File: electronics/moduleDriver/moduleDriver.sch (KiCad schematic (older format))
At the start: 31 parts, among them J1 Screw_Terminal_01x03, U1 Mega2560Shield, U10 ULN2003AModule, U11 ULN2003AModule, U12 ULN2003AModule, U13 ULN2003AModule, U14 SSD1306_I2C, U15 INA219_Breakout, U2 ULN2003AModule, U3 ULN2003AModule, U4 ULN2003AModule, U5 ULN2003AModule, U6 ULN2003AModule, U7 ULN2003AModule, U8 ULN2003AModule, U9 ULN2003AModule

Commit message: More schematic progress
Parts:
- removed JP?: 3V_VCC, symbol Device:Jumper_NO_Small
- removed JP?: 5V_VCC, symbol Device:Jumper_NO_Small
- added J?: Screw_Terminal_01x03, symbol Connector:Screw_Terminal_01x03
- added J? (x3): Conn_01x12_Male, symbol Connector:Conn_01x12_Male
- added R? (x12): 47k, symbol Device:R_Small
- added U?: RS485Module, symbol RS485Module:RS485Module
- added U?: LevelShifterModule, symbol LevelShifterModule:LevelShifterModule
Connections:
- net labels added: IOVCC, RS485_DRIVE_EN, RX_5V, TX_5V
- net labels removed: VCC
- wire segments 403 -> 517
- no-connect marks 49 -> 51
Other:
- note added: "IOVCC is sourced by (through) \nESP32 module when present."
- note added: "IOVCC is sourced by (through) \nMega 2560 when present."
- note added: "Resistors only for ESP32"
- moved on the sheet: J1, JP1, U1, U10, U11, U12, U13, U14, U15, U2, U3, U4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

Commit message: More schematic cleanup
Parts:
- added JP?: RX 3.3V, symbol Jumper:SolderJumper_2_Open
- added JP?: TX 3.3V, symbol Jumper:SolderJumper_2_Open
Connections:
- net RS485_DRIVE_EN: now also U?.5 (GPIO17), U?.5 (LV3); no longer U?.DE, U?.RE
- net RX: now also JP?.1 (A); no longer J?.2 (Pin_2), U1.D0
- net RX_5V: now also J?.2 (Pin_2), U1.D0, JP?.2 (B)
- net TX: now also JP?.1 (A); no longer J?.1 (Pin_1), U1.D1
- net TX_5V: now also J?.1 (Pin_1), U1.D1, JP?.2 (B)
- net RS485_DRIVE_EN_5V: now reaches U1.D4
- net RS485_DRIVE_EN_5V: now also U?.8 (HV3), U?.DE, U?.RE
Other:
- note added: "MCU Option 1: Mega2560 + SSD1306 OLED"
- note added: "MCU Option 2: TTGO T-Display (ESP32)"
- note added: "MCU Option 3: ESP32 D1 Mini"
- note added: "Motor Driver Modules"
- note added: "Only populate for shift register chaining"
- note added: "Optional: Current sense"
- note added: "Optional: RS485 comms/UART voltage shifting"
- note added: "Populate when using ESP32 MCU"
- note added: "Resistors only for ESP32\n(47k)"
- note added: "Sensor Connectors"
- note removed: "Resistors only for ESP32"
- moved on the sheet: JP1, U1, U14, U15, U?

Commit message: ESP32 D1 pinout connections
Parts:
- added J?: SR CHAIN IN, symbol Connector:Screw_Terminal_01x06
- added J?: SR CHAIN OUT, symbol Connector:Screw_Terminal_01x06
- J1: value Screw_Terminal_01x03 -> Power In
- J?: value Screw_Terminal_01x03 -> UART
- J?: value Conn_01x12_Male -> SENSOR
- J?: value Conn_01x12_Male -> IOVCC
- J?: value Conn_01x12_Male -> GND
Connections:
- net +5V: now also U?.36 (5V/5V)
- net CLOCK: now also U?.8 (GPIO18/D5), J?.2 (Pin_2)
- net CLOCK_IN: now also J?.2 (Pin_2)
- net DISP_BLK: now also U?.23 (GPIO27)
- net DISP_CLK: now also U?.25 (GPIO25)
- net DISP_CS: now also U?.33 (GPIO0)
- net DISP_DC: now also U?.27 (GPIO32)
- net DISP_MOSI: now also U?.18 (GPIO13)
- net DISP_RES: now also U?.31 (GPIO4), U?.9 (GPIO33)
- net GND: now also U?.1 (GND), U?.21 (GND), U?.34 (GND/GND)
- net IOVCC: now also U?.16 (3V3/3V3)
- net MOTOR_DATA: now also U?.12 (GPIO23/D7)
- net MOTOR_DATA_IN: now also J?.1 (Pin_1)
- net MOTOR_DATA_OUT: now also J?.1 (Pin_1)
- net MOTOR_LATCH: now also U?.6 (GPIO26/D0), J?.3 (Pin_3)
- net MOTOR_LATCH_IN: now also J?.3 (Pin_3)
- net MOTOR_OE: now also U?.32 (GPIO16/D4), J?.4 (Pin_4)
- net MOTOR_OE_IN: now also J?.4 (Pin_4)
- net RS485_DRIVE_EN: now also U?.30 (GPIO17/D3)
- net RX: now also U?.24 (GPIO3/RX)
- net SCL: now also U?.26 (GPIO22/D1)
- net SDA: now also U?.28 (GPIO21/D2)
- net SENSOR_DATA: now also U?.10 (GPIO19/D6), J?.5 (Pin_5)
- net SENSOR_DATA_IN: now also J?.5 (Pin_5)
- net SENSOR_LATCH: now also U?.14 (GPIO5/D8), J?.6 (Pin_6)
- net SENSOR_LATCH_IN: now also J?.6 (Pin_6)
- net TX: now also U?.22 (GPIO1/TX)
- no-connect marks 51 -> 57
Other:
- note added: "Connectors"
- note added: "ESP32/ESP8266 IO Support"
- note added: "MCU Option 3: ESP32/ESP8266 D1 Mini"
- note added: "Optional: Shift register chaining support"
- note removed: "MCU Option 3: ESP32 D1 Mini"
- note removed: "Only populate for shift register chaining"
- note removed: "Populate when using ESP32 MCU"
- moved on the sheet: J1, J?, JP?, R?, U10, U11, U12, U13, U15, U2, U3, U4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

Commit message: More schematic progress, comments
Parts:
- added JP4: Current Sense Bypass, symbol Device:Jumper_NO_Small
- J1: symbol Connector:Screw_Terminal_01x03 -> screw_terminal_01x03_power_output:Screw_Terminal_01x03
- gave numbers to parts that had none: 34
- renumbered U9 to U10, U15 to U11, U10 to U12, U11 to U13, U12 to U14, U13 to U15, U14 to U2, U2 to U3, U3 to U4, U4 to U5, U5 to U6, U6 to U7, U7 to U8, U8 to U9
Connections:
- net +3V3 is gone; now on net IOVCC: U16.3 (LV)
- net +12V: now also JP4.1
- net +12V_Monitored: now also JP4.2
- net +5V: now also U1.5V
- net IOVCC: now also U1.IOREF; no longer U1.5V
- net TX_5V: no longer J2.1 (Pin_1), U1.D1, U17.DI
- net RX_5V renamed RX_EXT
- new net TX_EXT: J2.1 (Pin_1), U1.D1, U17.DI
- no-connect marks 57 -> 81
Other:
- note added: "Configuration options:\n\nMega 2560: DNP U16; External RX/TX = 5V; do not use JP2/JP3\n\nESP32/ESP8266:\n For 5V RX/TX: Use U16; do not use JP2/JP3\n For 3.3V RX/TX: DNP U16; set JP2 and JP3"
- note added: "For compatibility with ESP8266, all critical IO\nuses the inner pins; optional IO (e.g. display)\ncan use the outer pins (only present for ESP32\nmodules)"
- note added: "IOVCC is sourced by\nESP32 module when present."
- note added: "IOVCC is sourced by\nMega 2560 when present."
- note added: "RS485 Requires 5V RX/TX - for ESP32/ESP8266 must use U16"
- note removed: "IOVCC is sourced by (through) \nESP32 module when present."
- note removed: "IOVCC is sourced by (through) \nMega 2560 when present."
- moved on the sheet: JP2, JP3, U16, U17

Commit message: Add some footprints and attach to schematic
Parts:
- added U30: ST7789_240x240, ST7789:ST7789_240x240, symbol LCD:ST7789_240x240
- J1, J2: footprint (none) -> TerminalBlock:TerminalBlock_bornier-3_P5.08mm
- J3, J4, J5: footprint (none) -> Connector_PinHeader_2.54mm:PinHeader_1x12_P2.54mm_Vertical
- J6, J7: footprint (none) -> TerminalBlock_TE-Connectivity:TerminalBlock_TE_282834-6_1x06_P2.54mm_Horizontal
- JP1, JP4: footprint (none) -> Connector_PinHeader_2.54mm:PinHeader_1x02_P2.54mm_Vertical
- JP2, JP3: footprint (none) -> Jumper:SolderJumper-2_P1.3mm_Open_RoundedPad1.0x1.5mm
- R1, R10, R11, R12, R2, R3, R4, R5, R6, R7, R8, R9: footprint (none) -> Resistor_THT:R_Axial_DIN0204_L3.6mm_D1.6mm_P1.90mm_Vertical
- U1: footprint (none) -> Mega2560Shield:Mega2560Shield
- U10, U12, U13, U14, U15, U3, U4, U5, U6, U7, U8, U9: footprint (none) -> ULN2003AModule:ULN2003AModule
- U18: footprint (none) -> ESP32:T-DISPLAY
- U2: footprint (none) -> Connector_PinSocket_2.54mm:PinSocket_1x04_P2.54mm_Vertical
- U20, U21: footprint MODULE -> Package_DIP:DIP-16_W7.62mm
- U22: value ST7789_IPS -> ST7789_80x160; footprint (none) -> ST7789:ST7789_80x160; symbol LCD:ST7789_IPS -> LCD:ST7789_80x160
- U23: footprint (none) -> ESP32:D1_32
- U24, U25, U26, U27, U28, U29: footprint (none) -> Package_DIP:DIP-16_W7.62mm
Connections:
- net +12V_Monitored: no longer U11.5 (VIN-)
- net DISP_BLK: now also U30.BLK
- net DISP_CLK: now also U30.SCL (SCL(CLK))
- net DISP_DC: now also U30.DC
- net DISP_MOSI: now also U30.SDA (SDA_(MOSI))
- net DISP_RES: now also U30.RES
- net GND: now also U30.GND
- net IOVCC: now also U30.VCC
- no-connect marks 81 -> 82
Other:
- note added: "47k. DNP for Mega 2560"
- note added: "IOVCC is sourced by the MCU\nmodule that's inserted, at the\nappropriate IO voltage\n(3.3V or 5V)"
- note removed: "IOVCC is sourced by\nESP32 module when present."
- note removed: "IOVCC is sourced by\nMega 2560 when present."
- note removed: "Resistors only for ESP32\n(47k)"
- moved on the sheet: U22

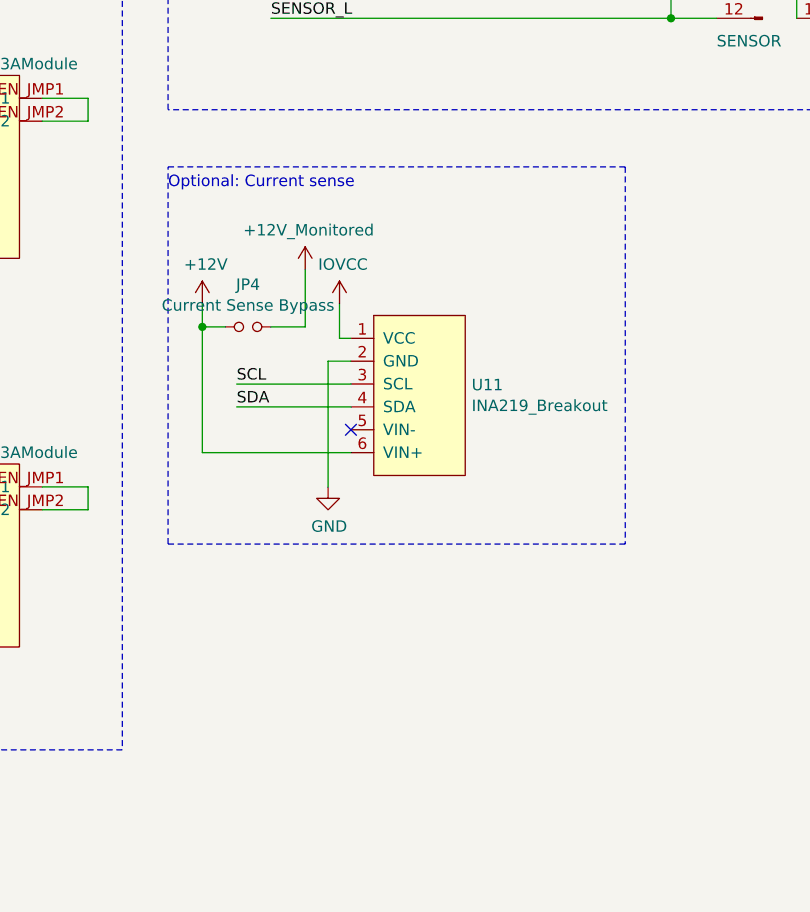
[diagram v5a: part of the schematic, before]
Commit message: Current sensor updates
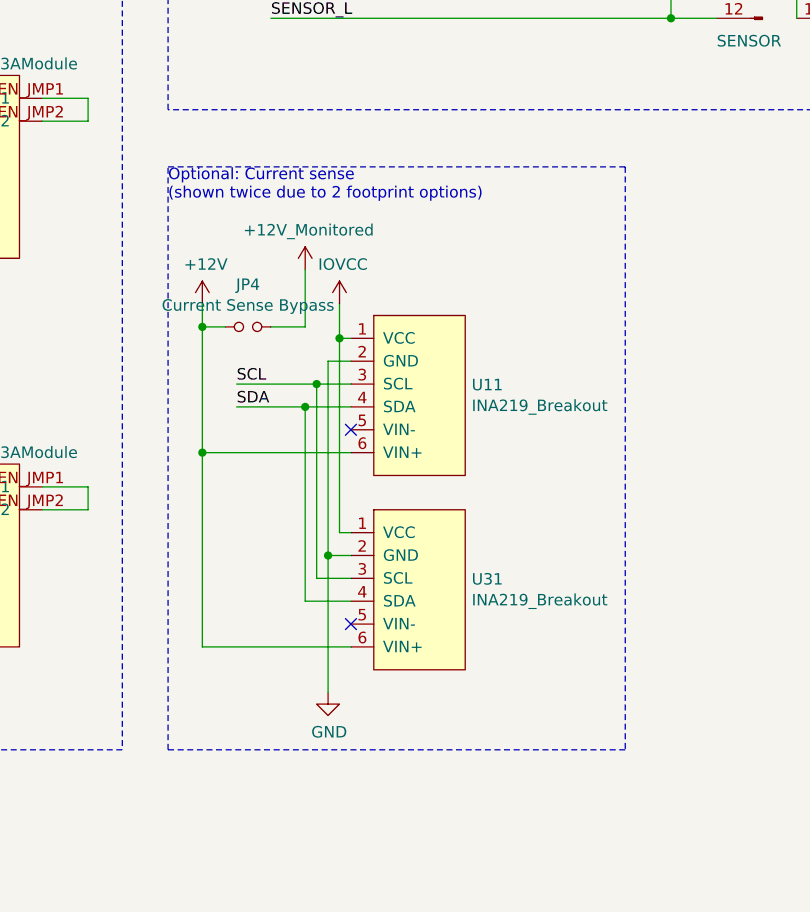
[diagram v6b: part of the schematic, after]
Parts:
- added U31: INA219_Breakout, INA219:INA219_SMALL, symbol INA219_Breakout:INA219_Breakout
- U11: footprint (none) -> INA219:INA219_SMALL
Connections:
- net +12V: now also U31.6 (VIN+)
- net GND: now also U31.2 (GND)
- net IOVCC: now also U31.1 (VCC)
- net SCL: now also U31.3 (SCL)
- net SDA: now also U31.4 (SDA)
- no-connect marks 82 -> 83
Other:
- note added: "Optional: Current sense\n(shown twice due to 2 footprint options)"
- note removed: "Optional: Current sense"
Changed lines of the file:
@@
 F 0 "U11" H 10528 5996 50  0000 L CNN
 F 1 "INA219_Breakout" H 10528 5905 50  0000 L CNN
-F 2 "" H 10000 6000 50  0001 C CNN
+F 2 "INA219:INA219_SMALL" H 10000 6000 50  0001 C CNN
 F 3 "" H 10000 6000 50  0001 C CNN
 	1    10300 5950
@@
 Wire Wire Line
 	10000 5800 9900 5800
-Wire Wire Line
-	9900 5800 9900 6350
 $Comp
 L power:GND #PWR035
 U 1 1 5F2DBE8C
-P 9900 6350
-F 0 "#PWR035" H 9900 6100 50  0001 C CNN
-F 1 "GND" H 9905 6177 50  0000 C CNN
-F 2 "" H 9900 6350 50  0001 C CNN
-F 3 "" H 9900 6350 50  0001 C CNN
-	1    9900 6350
+P 9900 7250
+F 0 "#PWR035" H 9900 7000 50  0001 C CNN
+F 1 "GND" H 9905 7077 50  0000 C CNN
+F 2 "" H 9900 7250 50  0001 C CNN
+F 3 "" H 9900 7250 50  0001 C CNN
+	1    9900 7250
 	1    0    0    -1
 $EndComp
@@
 SCL
 Wire Wire Line
-	10000 5900 9500 5900
-Wire Wire Line
-	10000 6000 9500 6000
+	10000 5900 9850 5900
+Wire Wire Line
+	10000 6000 9800 6000
 Text Label 19700 2800 2    50   ~ 0
 RX_EXT
@@
 Wire Notes Line
 	9200 4700 9200 2250
-Text Notes 9200 5050 0    50   ~ 0
-Optional: Current sense
+Text Notes 9200 5100 0    50   ~ 0
+Optional: Current sense\n(shown twice due to 2 footprint options)
 Wire Notes Line
 	9200 4950 11200 4950
-Wire Notes Line
-	11200 4950 11200 6600
-Wire Notes Line
-	11200 6600 9200 6600
-Wire Notes Line
-	9200 6600 9200 4950
 $Comp
 L Connector:Screw_Terminal_01x06 J6
@@
 	9800 5400 9800 5650
 Wire Wire Line
-	9350 6200 10000 6200
-Wire Wire Line
 	9350 5550 9350 5650
 $Comp
@@
 Wire Wire Line
 	20900 12750 20900 13300
+$Comp
+L INA219_Breakout:INA219_Breakout U31
+U 1 1 5FB8DCED
+P 10300 6800
+F 0 "U31" H 10528 6846 50  0000 L CNN
+F 1 "INA219_Breakout" H 10528 6755 50  0000 L CNN
+F 2 "INA219:INA219_SMALL" H 10000 6850 50  0001 C CNN
+F 3 "" H 10000 6850 50  0001 C CNN
+	1    10300 6800
+	1    0    0    -1
+$EndComp
+Wire Wire Line
+	9950 5700 9950 6550
+Wire Wire Line
+	9950 6550 10000 6550
+Connection ~ 9950 5700
+Wire Wire Line
+	9900 6650 10000 6650
+Wire Wire Line
+	9900 5800 9900 6650
+Wire Wire Line
+	9900 6650 9900 7250
+Connection ~ 9900 6650
+Wire Wire Line
+	9850 5900 9850 6750
+Wire Wire Line
+	9850 6750 10000 6750
+Connection ~ 9850 5900
+Wire Wire Line
+	9850 5900 9500 5900
+Wire Wire Line
+	9800 6000 9800 6850
+Wire Wire Line
+	9800 6850 10000 6850
+Connection ~ 9800 6000
+Wire Wire Line
+	9800 6000 9500 6000
+NoConn ~ 10000 6950
+Wire Wire Line
+	9350 6200 10000 6200
+Wire Wire Line
+	9350 6200 9350 7050
+Wire Wire Line
+	9350 7050 10000 7050
+Connection ~ 9350 6200
+Wire Notes Line
+	11200 4950 11200 7500
+Wire Notes Line
+	11200 7500 9200 7500
+Wire Notes Line
+	9200 7500 9200 4950
 $EndSCHEMATC

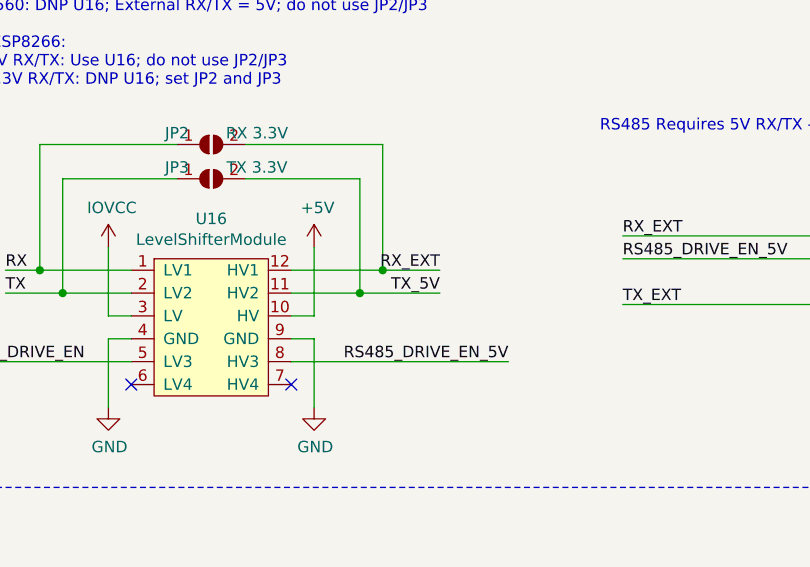
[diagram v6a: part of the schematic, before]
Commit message: Add RS485 module footprint
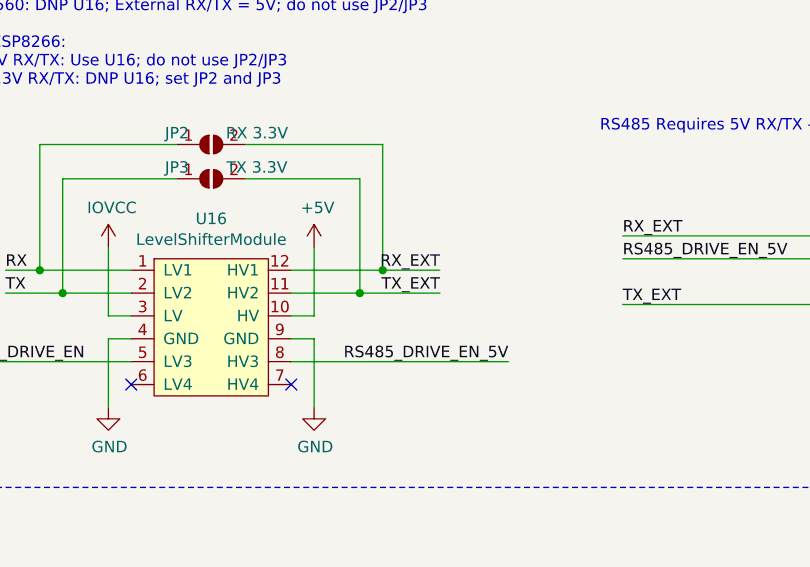
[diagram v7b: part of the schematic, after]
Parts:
- U17: footprint (none) -> RS485:RS485Module
- U19: footprint (none) -> Package_DIP:DIP-20_W7.62mm
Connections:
- net TX_5V is gone; now on net TX_EXT: JP3.2 (B), U16.11 (HV2)
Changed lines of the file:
@@
 F 0 "U19" H 7750 12950 50  0000 C CNN
 F 1 "74HC244" H 7850 12850 50  0000 C CNN
-F 2 "" H 7600 12200 50  0001 C CNN
+F 2 "Package_DIP:DIP-20_W7.62mm" H 7600 12200 50  0001 C CNN
 F 3 "http://www.nxp.com/documents/data_sheet/74HC_HCT244.pdf" H 7600 12200 50  0001 C CNN
 	1    7600 12200
@@
 F 0 "U17" H 5300 9815 50  0000 C CNN
 F 1 "RS485Module" H 5300 9724 50  0000 C CNN
-F 2 "" H 5300 9400 50  0001 C CNN
+F 2 "RS485:RS485Module" H 5300 9400 50  0001 C CNN
 F 3 "" H 5300 9400 50  0001 C CNN
 	1    5300 9400
@@
 RX_EXT
 Text Label 3050 9500 2    50   ~ 0
-TX_5V
+TX_EXT
 Wire Wire Line
 	1150 9400 1300 9400

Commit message: Progress
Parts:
- removed JP4: Current Sense Bypass, Connector_PinHeader_2.54mm:PinHeader_1x02_P2.54mm_Vertical, symbol Device:Jumper_NO_Small
- added C1, C10, C11, C12, C13, C14, C15, C16, C17, C18, C19, C2, C20, C21, C22, C5, C6, C7, C8, C9: 0.1uF, symbol Device:C_Small
- added C3: 100uF, symbol Device:CP_Small
- added C4: 10uF, symbol Device:CP_Small
- added H1, H2, H3, H4: MountingHole, MountingHole:MountingHole_4.3mm_M4_ISO7380, symbol Mechanical:MountingHole
- added J10: 12V SENSE, symbol Connector:Screw_Terminal_01x02
- added J11: Motor A, JST_XH_Connectors:JST_XH_2-5mm_5pin, symbol Connector:Conn_01x05_Male
- added J12: Motor E, JST_XH_Connectors:JST_XH_2-5mm_5pin, symbol Connector:Conn_01x05_Male
- added J13: Motor I, JST_XH_Connectors:JST_XH_2-5mm_5pin, symbol Connector:Conn_01x05_Male
- added J14: Motor B, JST_XH_Connectors:JST_XH_2-5mm_5pin, symbol Connector:Conn_01x05_Male
- added J15: Motor F, JST_XH_Connectors:JST_XH_2-5mm_5pin, symbol Connector:Conn_01x05_Male
- added J16: Motor J, JST_XH_Connectors:JST_XH_2-5mm_5pin, symbol Connector:Conn_01x05_Male
- added J17: Motor C, JST_XH_Connectors:JST_XH_2-5mm_5pin, symbol Connector:Conn_01x05_Male
- added J18: Motor G, JST_XH_Connectors:JST_XH_2-5mm_5pin, symbol Connector:Conn_01x05_Male
- added J19: Motor K, JST_XH_Connectors:JST_XH_2-5mm_5pin, symbol Connector:Conn_01x05_Male
- added J20: Motor D, JST_XH_Connectors:JST_XH_2-5mm_5pin, symbol Connector:Conn_01x05_Male
- added J21: Motor H, JST_XH_Connectors:JST_XH_2-5mm_5pin, symbol Connector:Conn_01x05_Male
- added J22: Motor L, JST_XH_Connectors:JST_XH_2-5mm_5pin, symbol Connector:Conn_01x05_Male
- added J8, J9: RS485, symbol Connector:Screw_Terminal_01x02
- added JP4: A0, Jumper:SolderJumper-2_P1.3mm_Open_TrianglePad1.0x1.5mm, symbol Jumper:SolderJumper_2_Open
- added JP5: A1, Jumper:SolderJumper-2_P1.3mm_Open_TrianglePad1.0x1.5mm, symbol Jumper:SolderJumper_2_Open
- added Q1, Q2: BSS138, Package_TO_SOT_SMD:SOT-23, symbol Transistor_FET:BSS138
- added R13, R14, R15, R16, R17, R18: 10k, Resistor_SMD:R_0805_2012Metric_Pad1.15x1.40mm_HandSolder, symbol Device:R_Small
- added R19: 0.1R 1% 1/2 W, Resistor_SMD:R_2512_6332Metric_Pad1.52x3.35mm_HandSolder, symbol Device:R_Small
- added U32: SP485, Package_SO:SOIC-8_3.9x4.9mm_P1.27mm, symbol Interface_UART:MAX485E
- added U33: INA219BxD, Package_SO:SOIC-8_3.9x4.9mm_P1.27mm, symbol Analog_ADC:INA219BxD
- added U34, U35, U36, U37, U38, U39, U40: TPL7407LA, Package_SO:SOIC-16_3.9x9.9mm_P1.27mm, symbol Transistor_Array:ULN2003A
- J1: symbol screw_terminal_01x03_power_output:Screw_Terminal_01x03 -> Connector:Screw_Terminal_01x03
- J6, J7: footprint TerminalBlock_TE-Connectivity:TerminalBlock_TE_282834-6_1x06_P2.54mm_Horizontal -> Connector_PinSocket_2.54mm:PinSocket_1x06_P2.54mm_Vertical
- JP2, JP3: footprint Jumper:SolderJumper-2_P1.3mm_Open_RoundedPad1.0x1.5mm -> Jumper:SolderJumper-2_P1.3mm_Open_TrianglePad1.0x1.5mm
- U11: value INA219_Breakout -> INA219 Breakout Wide (blue); footprint INA219:INA219_SMALL -> INA219:INA219_LARGE
- U16: footprint (none) -> LevelShifterModule:LevelShifterModule
- U31: value INA219_Breakout -> INA219 Breakout Narrow (purple)
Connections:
- net +12V: now also J1.1 (Pin_1), C3.1, J10.1 (Pin_1), R19.1, U33.8 (IN+); no longer U11.6 (VIN+), U31.6 (VIN+)
- net +12V_Monitored: now also C16.2, C17.2, C18.2, C19.2, C20.2, C21.2, C22.2, J10.2 (Pin_2), J11.5 (Pin_5), J12.5 (Pin_5), J13.5 (Pin_5), J14.5 (Pin_5), J15.5 (Pin_5), J16.5 (Pin_5), J17.5 (Pin_5), J18.5 (Pin_5), J19.5 (Pin_5), J20.5 (Pin_5), J21.5 (Pin_5), J22.5 (Pin_5), R19.2, U33.7 (IN-), U34.9 (COM), U35.9 (COM), U36.9 (COM), U37.9 (COM), U38.9 (COM), U39.9 (COM), U40.9 (COM); no longer J1.1 (Pin_1)
- net +5V: now also C1.2, C4.1, C6.2, R15.1, R16.1, U32.8 (VCC)
- net GND: now also U10.IN5, U10.IN6, U10.IN7, U12.IN5, U12.IN6, U12.IN7, U13.IN5, U13.IN6, U13.IN7, U14.IN5, U14.IN6, U14.IN7, U15.IN5, U15.IN6, U15.IN7, U3.IN5, U3.IN6, U3.IN7, U4.IN5, U4.IN6, U4.IN7, U5.IN5, U5.IN6, U5.IN7, U6.IN5, U6.IN6, U6.IN7, U7.IN5, U7.IN6, U7.IN7, U8.IN5, U8.IN6, U8.IN7, U9.IN5, U9.IN6, U9.IN7, C1.1, C10.2, C11.2, C12.2, C13.2, C14.2, C15.2, C16.1, C17.1, C18.1, C19.1, C2.1, C20.1, C21.1, C22.1, C3.2, C4.2, C5.1, C6.1, C7.2, C8.2, C9.2, R17.2, R18.2, U32.5 (GND), U33.6 (GND), U34.8 (GND), U35.8 (GND), U36.8 (GND), U37.8 (GND), U38.8 (GND), U39.7 (I7), U39.8 (GND), U40.8 (GND)
- net IOVCC: now also C10.1, C11.1, C12.1, C13.1, C14.1, C15.1, C2.2, C5.2, C7.1, C8.1, C9.1, JP4.1 (A), JP5.1 (A), Q1.1 (G), Q2.1 (G), R13.1, R14.1, U33.5 (VS)
- net MOTOR_A_PHASE_A: now also U34.1 (I1)
- net MOTOR_A_PHASE_B: now also U34.2 (I2)
- net MOTOR_A_PHASE_C: now also U34.3 (I3)
- net MOTOR_A_PHASE_D: now also U34.4 (I4)
- net MOTOR_B_PHASE_A: now also U34.5 (I5)
- net MOTOR_B_PHASE_B: now also U34.6 (I6)
- net MOTOR_B_PHASE_C: now also U34.7 (I7)
- net MOTOR_B_PHASE_D: now also U36.1 (I1)
- net MOTOR_C_PHASE_A: now also U36.2 (I2)
- net MOTOR_C_PHASE_B: now also U36.3 (I3)
- net MOTOR_C_PHASE_C: now also U36.4 (I4)
- net MOTOR_C_PHASE_D: now also U36.5 (I5)
- net MOTOR_D_PHASE_A: now also U36.6 (I6)
- net MOTOR_D_PHASE_B: now also U36.7 (I7)
- net MOTOR_D_PHASE_C: now also U38.1 (I1)
- net MOTOR_D_PHASE_D: now also U38.2 (I2)
- net MOTOR_E_PHASE_A: now also U38.3 (I3)
- net MOTOR_E_PHASE_B: now also U38.4 (I4)
- net MOTOR_E_PHASE_C: now also U38.5 (I5)
- net MOTOR_E_PHASE_D: now also U38.6 (I6)
- net MOTOR_F_PHASE_A: now also U38.7 (I7)
- net MOTOR_F_PHASE_B: now also U40.1 (I1)
- net MOTOR_F_PHASE_C: now also U40.2 (I2)
- net MOTOR_F_PHASE_D: now also U40.3 (I3)
- net MOTOR_G_PHASE_A: now also U40.4 (I4)
- net MOTOR_G_PHASE_B: now also U40.5 (I5)
- net MOTOR_G_PHASE_C: now also U40.6 (I6)
- net MOTOR_G_PHASE_D: now also U40.7 (I7)
- net MOTOR_H_PHASE_A: now also U35.1 (I1)
- net MOTOR_H_PHASE_B: now also U35.2 (I2)
- net MOTOR_H_PHASE_C: now also U35.3 (I3)
- net MOTOR_H_PHASE_D: now also U35.4 (I4)
- net MOTOR_I_PHASE_A: now also U35.5 (I5)
- net MOTOR_I_PHASE_B: now also U35.6 (I6)
- net MOTOR_I_PHASE_C: now also U35.7 (I7)
- net MOTOR_I_PHASE_D: now also U37.1 (I1)
- net MOTOR_J_PHASE_A: now also U37.2 (I2)
- net MOTOR_J_PHASE_B: now also U37.3 (I3)
- net MOTOR_J_PHASE_C: now also U37.4 (I4)
- net MOTOR_J_PHASE_D: now also U37.5 (I5)
- net MOTOR_K_PHASE_A: now also U37.6 (I6)
- net MOTOR_K_PHASE_B: now also U37.7 (I7)
- net MOTOR_K_PHASE_C: now also U39.1 (I1)
- net MOTOR_K_PHASE_D: now also U39.2 (I2)
- net MOTOR_L_PHASE_A: now also U39.3 (I3)
- net MOTOR_L_PHASE_B: now also U39.4 (I4)
- net MOTOR_L_PHASE_C: now also U39.5 (I5)
- net MOTOR_L_PHASE_D: now also U39.6 (I6)
- net RS485_DRIVE_EN: now also U1.D4, U17.DE, U17.RE, U32.2 (~RE), U32.3 (DE); no longer U16.5 (LV3)
- net RX: now also Q1.2 (S), R13.2
- net RX_EXT: now also Q1.3 (D), R15.2, U32.1 (RO)
- net SCL: now also U18.8 (GPIO13), U33.4 (SCL); no longer U18.21 (GPIO38)
- net SDA: now also U18.6 (GPIO2), U33.3 (SDA); no longer U18.22 (GPIO37)
- net TX: now also Q2.2 (S), R14.2
- net TX_EXT: now also Q2.3 (D), R16.2, U32.4 (DI)
- removed net RS485_DRIVE_EN_5V: U1.D4, U16.8 (HV3), U17.DE, U17.RE
- new net: J8.2 (Pin_2), J9.2 (Pin_2), U32.6 (A)
- new net: J8.1 (Pin_1), J9.1 (Pin_1), U32.7 (B)
- new net: JP5.2 (B), R18.1, U33.1 (A1)
- new net: JP4.2 (B), R17.1, U33.2 (A0)
- new net OUT_A_PHASE_A: J11.1 (Pin_1), U34.16 (O1)
- new net OUT_A_PHASE_B: J11.2 (Pin_2), U34.15 (O2)
- new net OUT_A_PHASE_C: J11.3 (Pin_3), U34.14 (O3)
- new net OUT_A_PHASE_D: J11.4 (Pin_4), U34.13 (O4)
- new net OUT_B_PHASE_A: J14.1 (Pin_1), U34.12 (O5)
- new net OUT_B_PHASE_B: J14.2 (Pin_2), U34.11 (O6)
- new net OUT_B_PHASE_C: J14.3 (Pin_3), U34.10 (O7)
- new net OUT_B_PHASE_D: J14.4 (Pin_4), U36.16 (O1)
- new net OUT_C_PHASE_A: J17.1 (Pin_1), U36.15 (O2)
- new net OUT_C_PHASE_B: J17.2 (Pin_2), U36.14 (O3)
- new net OUT_C_PHASE_C: J17.3 (Pin_3), U36.13 (O4)
- new net OUT_C_PHASE_D: J17.4 (Pin_4), U36.12 (O5)
- new net OUT_D_PHASE_A: J20.1 (Pin_1), U36.11 (O6)
- new net OUT_D_PHASE_B: J20.2 (Pin_2), U36.10 (O7)
- new net OUT_D_PHASE_C: J20.3 (Pin_3), U38.16 (O1)
- new net OUT_D_PHASE_D: J20.4 (Pin_4), U38.15 (O2)
- new net OUT_E_PHASE_A: J12.1 (Pin_1), U38.14 (O3)
- new net OUT_E_PHASE_B: J12.2 (Pin_2), U38.13 (O4)
- new net OUT_E_PHASE_C: J12.3 (Pin_3), U38.12 (O5)
- new net OUT_E_PHASE_D: J12.4 (Pin_4), U38.11 (O6)
- new net OUT_F_PHASE_A: J15.1 (Pin_1), U38.10 (O7)
- new net OUT_F_PHASE_B: J15.2 (Pin_2), U40.16 (O1)
- new net OUT_F_PHASE_C: J15.3 (Pin_3), U40.15 (O2)
- new net OUT_F_PHASE_D: J15.4 (Pin_4), U40.14 (O3)
- new net OUT_G_PHASE_A: J18.1 (Pin_1), U40.13 (O4)
- new net OUT_G_PHASE_B: J18.2 (Pin_2), U40.12 (O5)
- new net OUT_G_PHASE_C: J18.3 (Pin_3), U40.11 (O6)
- new net OUT_G_PHASE_D: J18.4 (Pin_4), U40.10 (O7)
- new net OUT_H_PHASE_A: J21.1 (Pin_1), U35.16 (O1)
- new net OUT_H_PHASE_B: J21.2 (Pin_2), U35.15 (O2)
- new net OUT_H_PHASE_C: J21.3 (Pin_3), U35.14 (O3)
- new net OUT_H_PHASE_D: J21.4 (Pin_4), U35.13 (O4)
- new net OUT_I_PHASE_A: J13.1 (Pin_1), U35.12 (O5)
- new net OUT_I_PHASE_B: J13.2 (Pin_2), U35.11 (O6)
- new net OUT_I_PHASE_C: J13.3 (Pin_3), U35.10 (O7)
- new net OUT_I_PHASE_D: J13.4 (Pin_4), U37.16 (O1)
- new net OUT_J_PHASE_A: J16.1 (Pin_1), U37.15 (O2)
- new net OUT_J_PHASE_B: J16.2 (Pin_2), U37.14 (O3)
- new net OUT_J_PHASE_C: J16.3 (Pin_3), U37.13 (O4)
- new net OUT_J_PHASE_D: J16.4 (Pin_4), U37.12 (O5)
- new net OUT_K_PHASE_A: J19.1 (Pin_1), U37.11 (O6)
- new net OUT_K_PHASE_B: J19.2 (Pin_2), U37.10 (O7)
- new net OUT_K_PHASE_C: J19.3 (Pin_3), U39.16 (O1)
- new net OUT_K_PHASE_D: J19.4 (Pin_4), U39.15 (O2)
- new net OUT_L_PHASE_A: J22.1 (Pin_1), U39.14 (O3)
- new net OUT_L_PHASE_B: J22.2 (Pin_2), U39.13 (O4)
- new net OUT_L_PHASE_C: J22.3 (Pin_3), U39.12 (O5)
- new net OUT_L_PHASE_D: J22.4 (Pin_4), U39.11 (O6)
- no-connect marks 83 -> 52
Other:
- note added: "3A minimum rating, 5A+ preferred"
- note added: "Optional: Current sense\n\nTo omit, install a jumper wire across 12V SENSE.\n\nThere are 3 options:\n- "Adafruit-style" wide module (blue)\n- narrow module (purple)\n- populate IC and supporting components directly on PCB\n\nFor modules, install wires from screw terminals\non the module to 12V SENSE screw terminals: \nVIN+ to VIN+ & VIN- to VIN-\n\n12V SENSE is unused with populated IC."
- note added: "RS485 Requires 5V RX/TX - for ESP32/ESP8266 must use level shifter"
- note added: "TODO: bypass capacitors"
- note added: "VIN- and VIN+ are not connected via module\nheaders because max current is near the limit\nof pin headers. Use screw terminals instead."
- note removed: "Optional: Current sense\n(shown twice due to 2 footprint options)"
- note removed: "RS485 Requires 5V RX/TX - for ESP32/ESP8266 must use U16"
- moved on the sheet: JP2, JP3, U11, U16, U17, U31
